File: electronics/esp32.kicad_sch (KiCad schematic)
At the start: 32 parts, among them J2 Conn_01x03, J4 Conn_02x02_Odd_Even, SW1 SW_Push, SW2 SW_Push, U5 ESP32-S3-WROOM-1, U9 W25Q16JVSS, Y1 FC-135_32.7680KA-A0

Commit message: Add current-sense amplifier offset and fix first-boot download mode
Improve measurement accuracy near zero and enable bidirectional current sensing by adding the current-sense amplifier offset.

Resolve the download-mode issue encountered on first boot.

Signed-off-by: Maxim Pavlov <max.eelabs@gmail.com>
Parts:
- C16: now not fitted; now left out of the parts list
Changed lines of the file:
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@@
 		(title "PSU-EXT ESP-32")
 		(date "2026-08-08")
-		(rev "1.2.0")
+		(rev "1.2.1")
 		(company "MaxEELabs")
 		(comment 3 "This hardware design is licensed under CERN-OHL-S v2.\nCopyright © 2026 PSU-EXT Authors: https://github.com/PSU-Ext-Org/psu-ext")
@@
 	)
 	(junction
-		(at 199.39 91.44)
-		(diameter 0)
-		(color 0 0 0 0)
-	)
-	(junction
 		(at 196.85 132.08)
 		(diameter 0)
@@
 	)
 	(junction
+		(at 199.39 91.44)
+		(diameter 0)
+		(color 0 0 0 0)
+	)
+	(junction
 		(at 48.26 33.02)
 		(diameter 0)
@@
 		(body_style 1)
 		(exclude_from_sim no)
-		(in_bom yes)
+		(in_bom no)
 		(on_board yes)
-		(in_pos_files yes)
-		(dnp no)
+		(in_pos_files no)
+		(dnp yes)
 		(property "Reference" "C16"
 			(at 183.134 98.806 90)

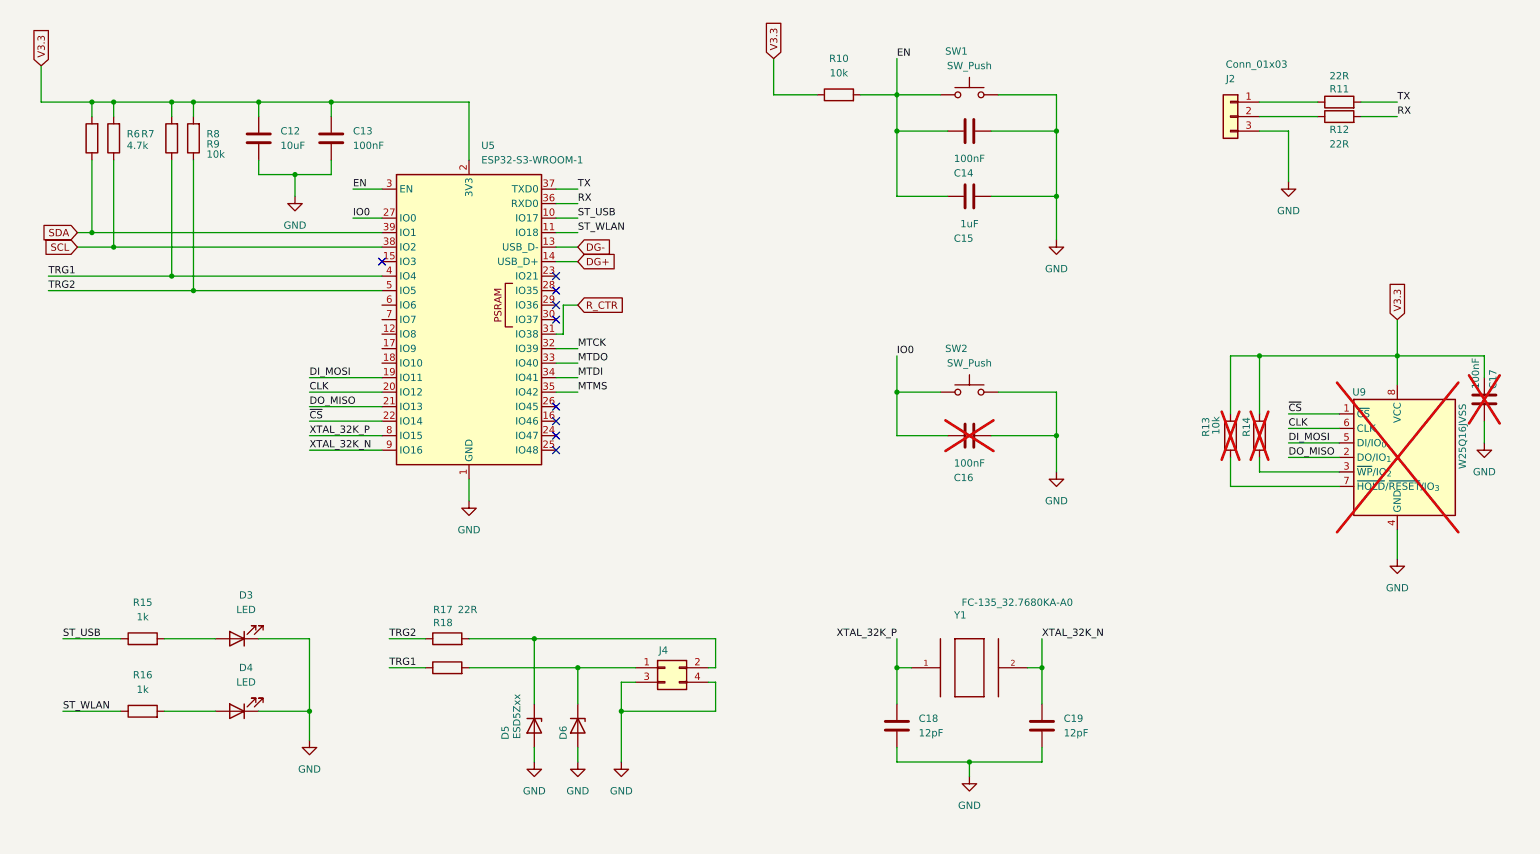
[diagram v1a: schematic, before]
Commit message: Added input buffernig and negative rail for near-zero measurments
Added I2C_NUM_1 on IO6 (SDA) and IO7 (SCL).

Signed-off-by: Maxim Pavlov <max.eelabs@gmail.com>
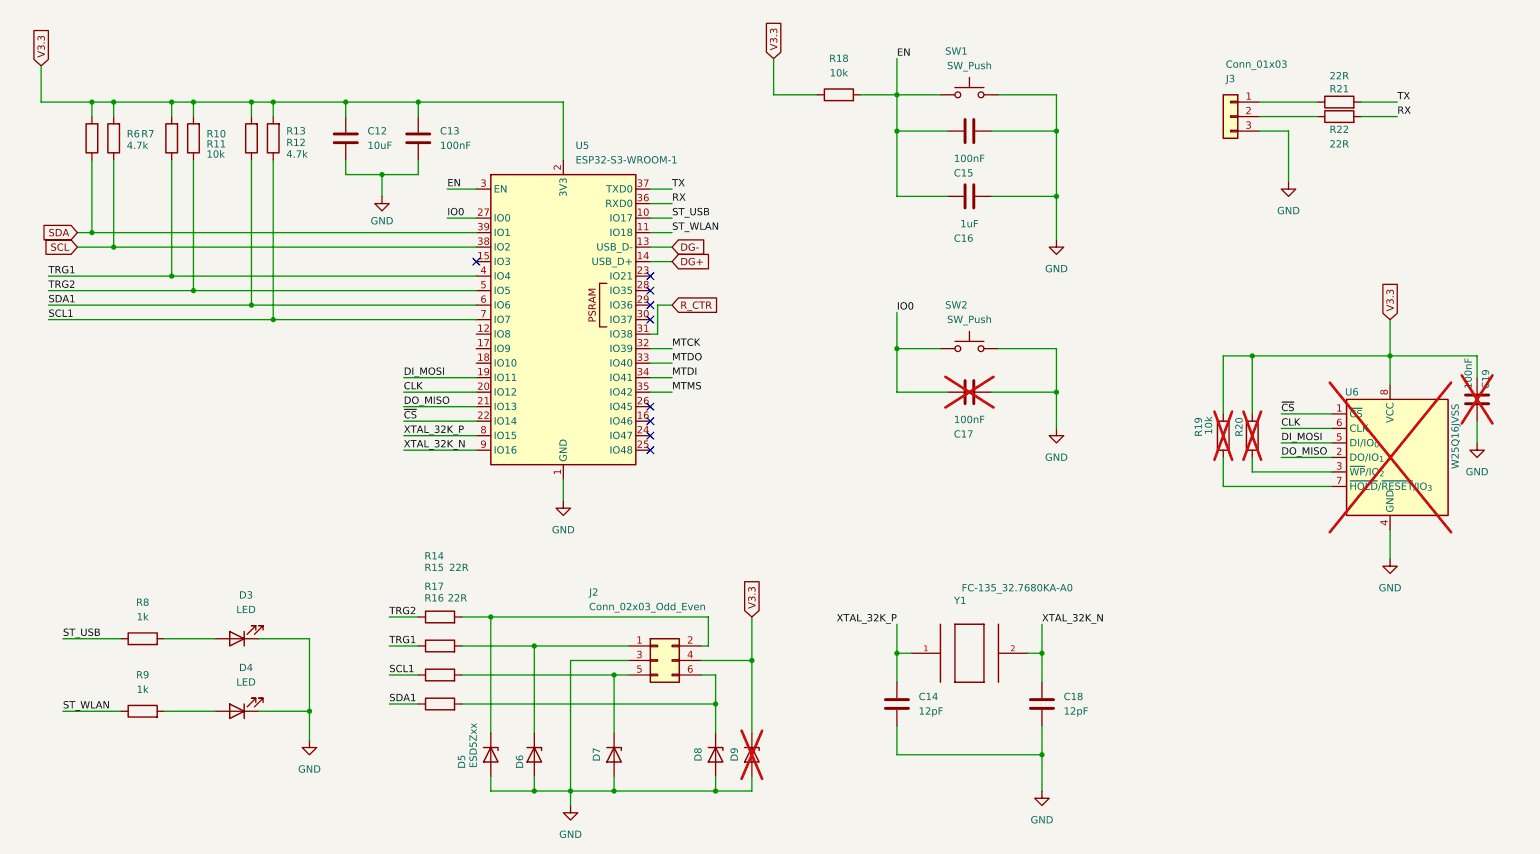
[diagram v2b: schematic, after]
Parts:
- removed J4: Conn_02x02_Odd_Even, Connector_PinHeader_2.54mm:PinHeader_2x02_P2.54mm_Vertical, symbol Connector_Generic:Conn_02x02_Odd_Even
- added D7, D8, D9: ESD5Zxx, Diode_SMD:D_SOD-523, symbol Diode:ESD5Zxx
- added J2: Conn_02x03_Odd_Even, Connector_PinHeader_2.54mm:PinHeader_2x03_P2.54mm_Vertical, symbol Connector_Generic:Conn_02x03_Odd_Even
- added R12, R13: 4.7k, Resistor_SMD:R_0805_2012Metric, symbol Device:R
- added R16, R17: 22R, Resistor_SMD:R_0805_2012Metric, symbol Device:R
- renumbered C18 to C14, C14 to C15, C15 to C16, C16 to C17, C19 to C18, C17 to C19, J2 to J3, R8 to R10, R9 to R11, R17 to R14, R18 to R15, R10 to R18, R13 to R19, R14 to R20, R11 to R21, R12 to R22, R15 to R8, R16 to R9, U9 to U6
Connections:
- net GND: now also D7.2 (A), D8.2 (A), D9.2 (A), J2.3 (Pin_3)
- net V3.3: now also D9.1 (K), J2.4 (Pin_4), R12.2, R13.2
- net at D6.1 (K), R15.2: now also J2.1 (Pin_1)
- net SDA1: now reaches U5.6 (IO6)
- net SDA1: now also R12.1, R17.1
- net SCL1: now reaches U5.7 (IO7)
- net SCL1: now also R13.1, R16.1
- net at D5.1 (K), R14.2: now also J2.2 (Pin_2)
- new net: D8.1 (K), J2.6 (Pin_6), R17.2
- new net: D7.1 (K), J2.5 (Pin_5), R16.2
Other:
- moved on the sheet: C12, C13, C14, C17, C18, C19, D5, D6, R14, R15, R19, R20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

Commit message: Added IO3 pullup and negative 3V3 rail testpoint, few other PCB laypu… (#4)
* Added IO3 pullup and negative 3V3 rail testpoint, few other PCB layput improvements.
* Updated exports - gerbers, schematics, bom, CPL KiCad for version 1.3.1

---------

Signed-off-by: Maxim Pavlov <max.eelabs@gmail.com>
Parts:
- added R14: 10k, Resistor_SMD:R_0805_2012Metric, symbol Device:R
- D5, D6, D7, D8: value ESD5Zxx -> ESD5Z3.3T1G
- D9: value ESD5Zxx -> ESD5Z3.3T1G; now left out of the parts list
- R22: renamed from R21; now not fitted; now left out of the parts list
- R23: renamed from R22; now not fitted; now left out of the parts list
- renumbered R14 to R15, R15 to R16, R16 to R17, R17 to R18, R18 to R19, R19 to R20, R20 to R21
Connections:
- net V3.3: now also R14.2
- net at U5.15 (IO3): now also R14.1
- no-connect marks 9 -> 8
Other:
- moved on the sheet: C12, C13, R10, R11, R12, R13, R6, R7
